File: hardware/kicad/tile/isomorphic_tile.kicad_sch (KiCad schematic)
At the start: 8 parts, among them J101 Conn_LEFT, J102 Conn_TOP, J103 Conn_BOTTOM, J104 Conn_RIGHT, J105 BTNs_L_MSB, J106 BTNs_L_LSB, J107 BTNs_MSB, J108 BTNs_LSB

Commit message: KiCad: rename Italian field and footprint names
- Symbol field "Codice" (manufacturer part number) -> "MPN".
- Mouse-bite footprint "Senza-titolo" -> "MouseBite_NPTH_0.5mm".

Verified: netlist identical to rev A, switch/connector/outline
invariants OK, DRC report counts unchanged.
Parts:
- J101, J102: Codice 613010143121 -> (none); MPN (none) -> 613010143121
- J103, J104: Codice 61300811021 -> (none); MPN (none) -> 61300811021
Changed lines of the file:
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@@
 			)
 		)
-		(property "Codice" "613010143121"
+		(property "MPN" "613010143121"
 			(at 87.63 69.85 90)
 			(effects
@@
 			)
 		)
-		(property "Codice" "613010143121"
+		(property "MPN" "613010143121"
 			(at 36.83 120.65 0)
 			(effects
@@
 			)
 		)
-		(property "Codice" "61300811021"
+		(property "MPN" "61300811021"
 			(at 140.97 120.65 0)
 			(effects
@@
 			)
 		)
-		(property "Codice" "61300811021"
+		(property "MPN" "61300811021"
 			(at 87.63 173.99 90)
 			(effects

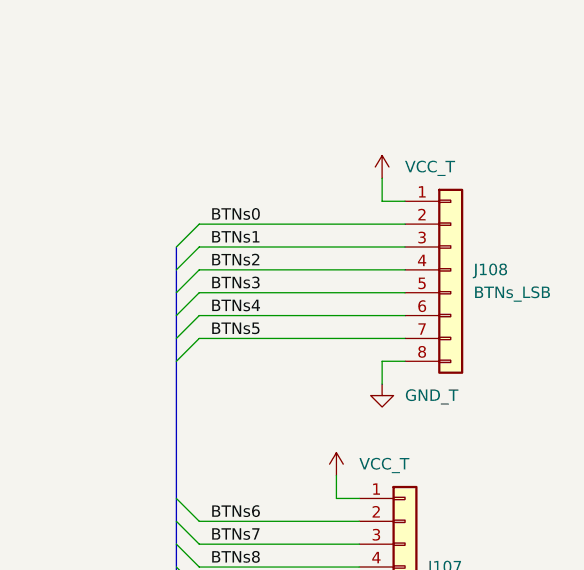
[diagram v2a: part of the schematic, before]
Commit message: Rev B schematic: series termination, decoupling, assembly-ready parts
Function unchanged (no logic connection changes). Applied by
hardware/kicad/tile/scripts/revb_schematic.py:

- 33 ohm series resistors R201-R207 at every driver leaving the tile
  (L_clk, T_clk, L_latch, T_latch, B_data, R_data, B_W).
- 100 nF per logic IC (C201-C209); PWR_FLAGs on VCC, GND, VCC_T, GND_T.
- Values match the ordered parts (74LVC..., 74HC161); footprints:
  0603 passives, TI DCT land pattern for the 2G parts, standard
  SOT-23-5, SMD bulk capacitor, Kailh MX hot-swap sockets; Manufacturer
  and MPN fields, Link field dropped.
- Project footprint library with the hot-swap socket from
  keyswitch-kicad-library v2.3 (CC-BY-SA 4.0 with design exception).

Verified: netlist identical to rev A after collapsing R201-R207 and
ignoring C201-C209; ERC 0 errors (was 4).
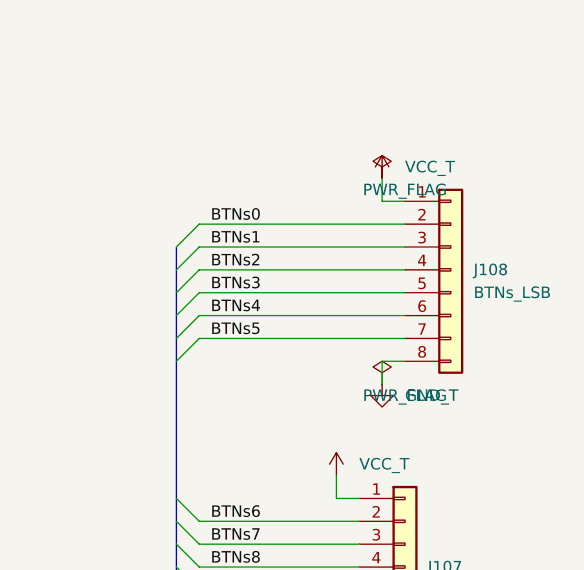
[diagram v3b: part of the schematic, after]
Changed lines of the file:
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@@
+		)
+	)
+	(symbol
+		(lib_id "power:PWR_FLAG")
+		(at 238.76 44.45 0)
+		(unit 1)
+		(body_style 1)
+		(exclude_from_sim no)
+		(in_bom yes)
+		(on_board yes)
+		(in_pos_files yes)
+		(dnp no)
+		(fields_autoplaced yes)
+		(property "Reference" "#FLG0203"
+			(at 241.3 43.18 0)
+			(hide yes)
+			(show_name no)
+			(do_not_autoplace no)
+			(effects
+				(font
+					(size 1.27 1.27)
+				)
+			)
+		)
+		(property "Value" "PWR_FLAG"
+			(at 241.3 45.72 0)
+			(show_name no)
+			(do_not_autoplace no)
+			(effects
+				(font
+					(size 1.27 1.27)
+				)
+			)
+		)
+		(property "Footprint" ""
+			(at 238.76 44.45 0)
+			(hide yes)
+			(show_name no)
+			(do_not_autoplace no)
+			(effects
+				(font
+					(size 1.27 1.27)
+				)
+			)
+		)
+		(property "Datasheet" ""
+			(at 238.76 44.45 0)
+			(hide yes)
+			(show_name no)
+			(do_not_autoplace no)
+			(effects
+				(font
+					(size 1.27 1.27)
+				)
+			)
+		)
+		(property "Description" "Special symbol for telling ERC where power comes from"
+			(at 238.76 44.45 0)
+			(hide yes)
+			(show_name no)
+			(do_not_autoplace no)
+			(effects
+				(font
+					(size 1.27 1.27)
+				)
+			)
+		)
+		(pin "1"
+		)
+		(instances
+			(project "isomorphic_tile"
+				(path "/2a6329ec-b0e8-4012-8f5a-476608b8b2cc"
+					(reference "#FLG0203")
+					(unit 1)
+				)
+			)
+		)
+	)
+	(symbol
+		(lib_id "power:PWR_FLAG")
+		(at 238.76 67.31 0)
+		(unit 1)
+		(body_style 1)
+		(exclude_from_sim no)
+		(in_bom yes)
+		(on_board yes)
+		(in_pos_files yes)
+		(dnp no)
+		(fields_autoplaced yes)
+		(property "Reference" "#FLG0204"
+			(at 241.3 66.04 0)
+			(hide yes)
+			(show_name no)
+			(do_not_autoplace no)
+			(effects
+				(font
+					(size 1.27 1.27)
+				)
+			)
+		)
+		(property "Value" "PWR_FLAG"
+			(at 241.3 68.58 0)
+			(show_name no)
+			(do_not_autoplace no)
+			(effects
+				(font
+					(size 1.27 1.27)
+				)
+			)
+		)
+		(property "Footprint" ""
+			(at 238.76 67.31 0)
+			(hide yes)
+			(show_name no)
+			(do_not_autoplace no)
+			(effects
+				(font
+					(size 1.27 1.27)
+				)
+			)
+		)
+		(property "Datasheet" ""
+			(at 238.76 67.31 0)
+			(hide yes)
+			(show_name no)
+			(do_not_autoplace no)
+			(effects
+				(font
+					(size 1.27 1.27)
+				)
+			)
+		)
+		(property "Description" "Special symbol for telling ERC where power comes from"
+			(at 238.76 67.31 0)
+			(hide yes)
+			(show_name no)
+			(do_not_autoplace no)
+			(effects
+				(font
+					(size 1.27 1.27)
+				)
+			)
+		)
+		(pin "1"
+		)
+		(instances
+			(project "isomorphic_tile"
+				(path "/2a6329ec-b0e8-4012-8f5a-476608b8b2cc"
+					(reference "#FLG0204")
+					(unit 1)
+				)
+			)
 		)
 	)
